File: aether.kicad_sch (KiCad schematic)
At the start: 4 parts, among them U1 LoRa-E5

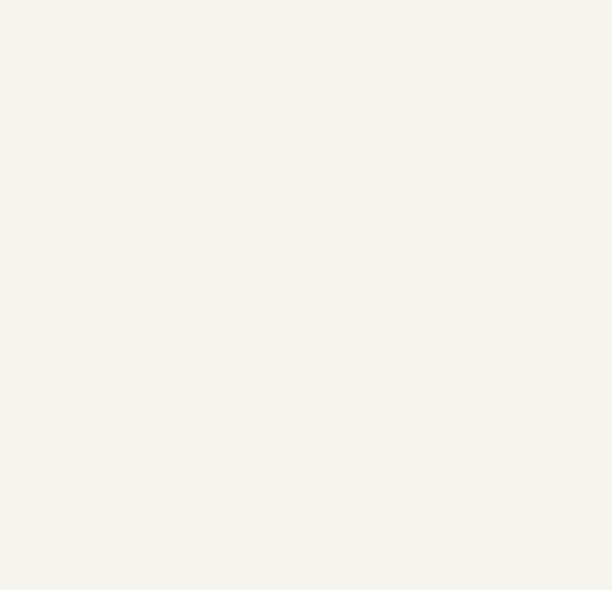
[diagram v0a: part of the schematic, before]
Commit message: Reorganized repo & added power schematic
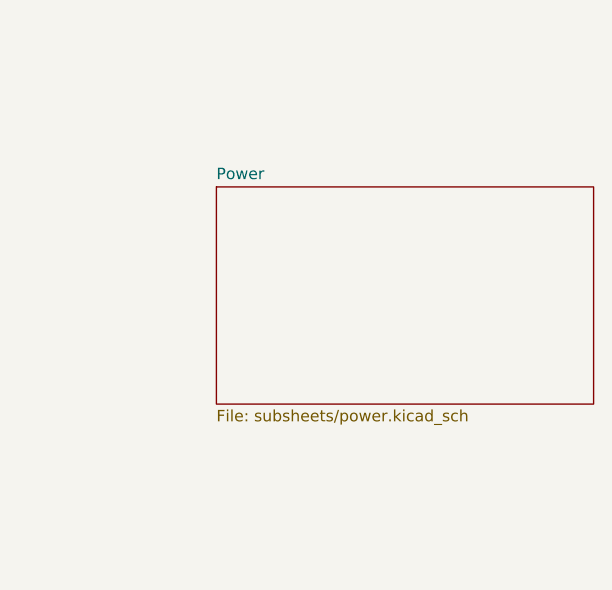
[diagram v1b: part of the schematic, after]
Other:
- added sheet Power (subsheets/power.kicad_sch)

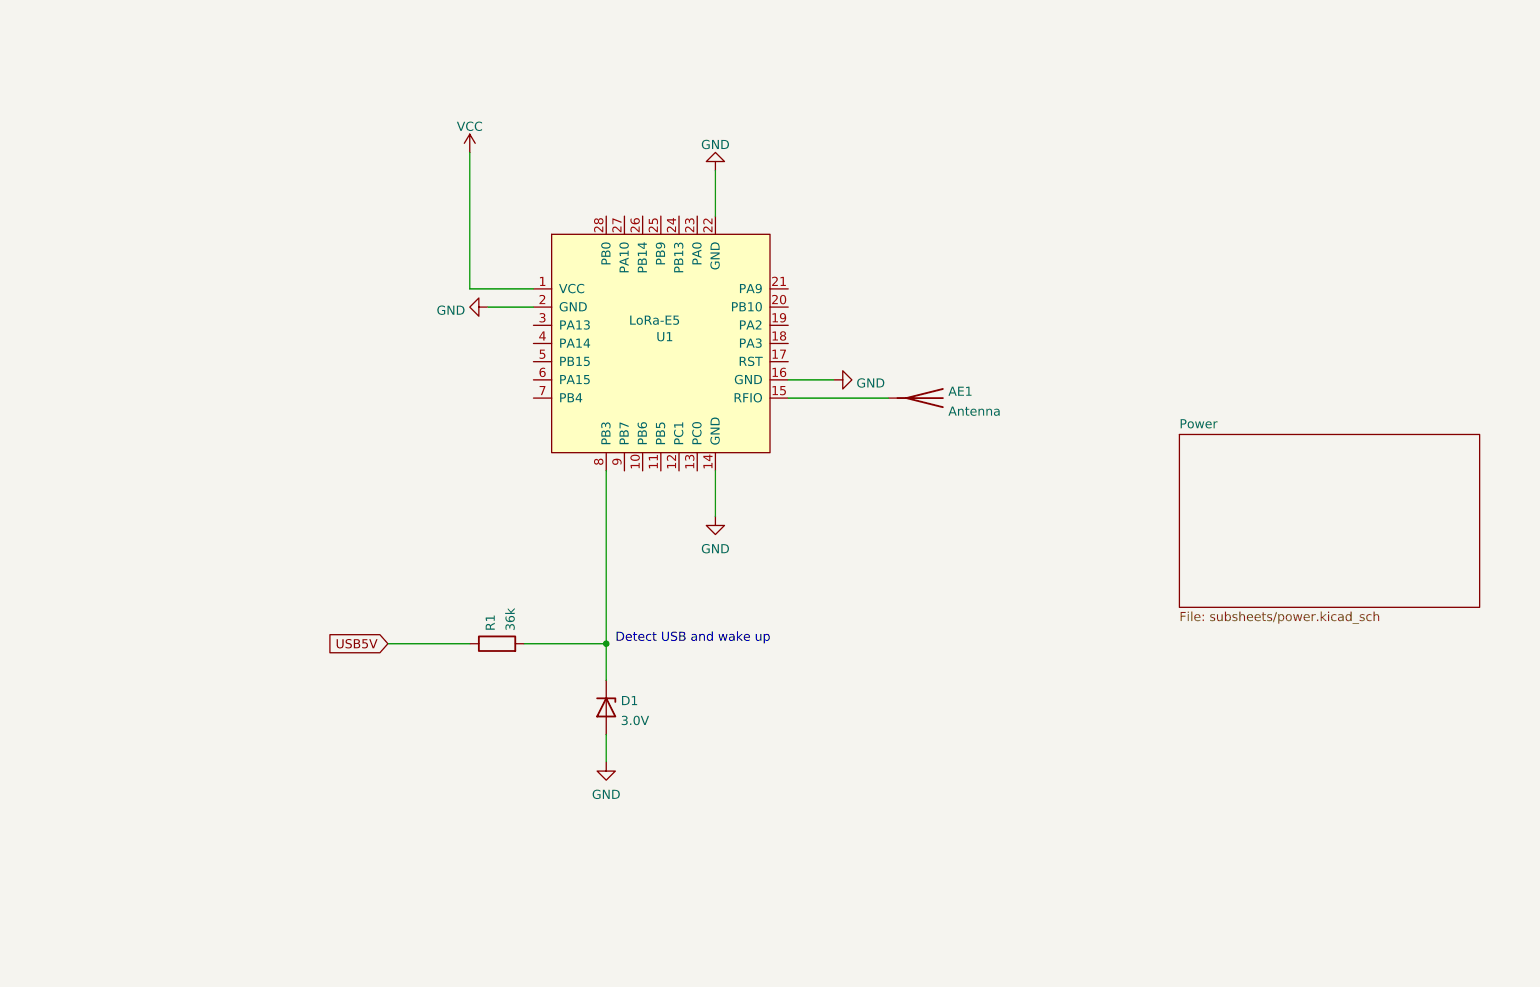
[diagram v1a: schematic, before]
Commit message: Added MCU sch sheet and updated sheet layout
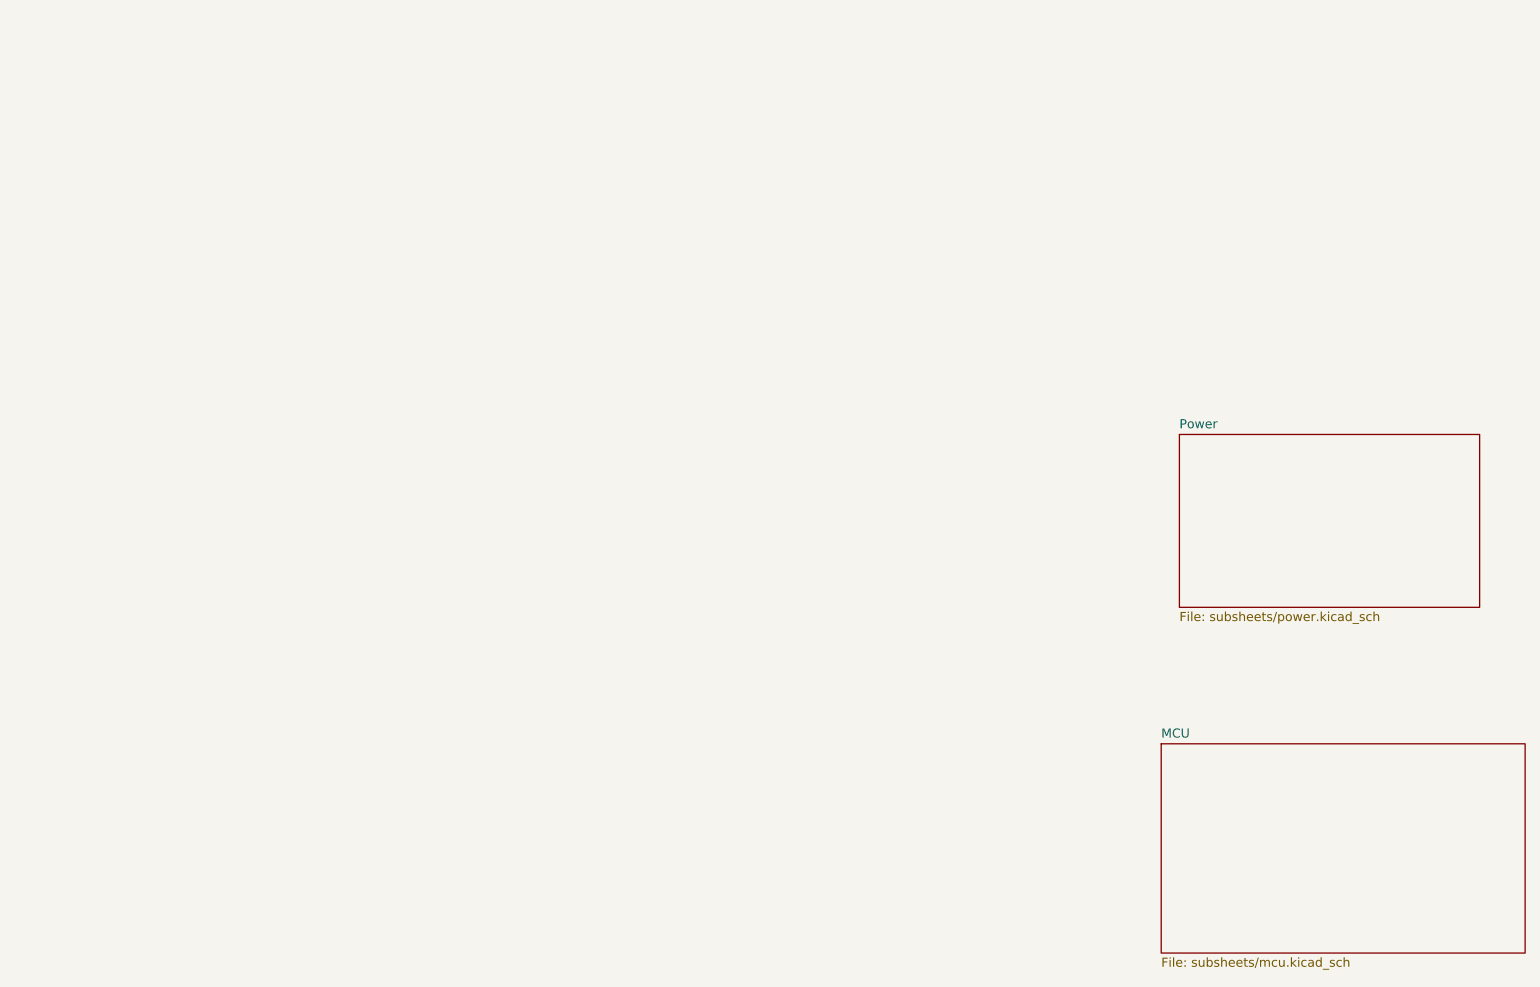
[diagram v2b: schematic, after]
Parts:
- removed AE1: Antenna, symbol Device:Antenna
- removed D1: 3.0V, symbol Device:D_Zener
- removed R1: 36k, symbol Device:R
- removed U1: LoRa-E5, symbol LoRa-E5:LoRa-E5
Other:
- added sheet MCU (subsheets/mcu.kicad_sch)
- note removed: "Detect USB and wake up"
- title: Aether Sensor Network - LoRa Module -> LoRa Module

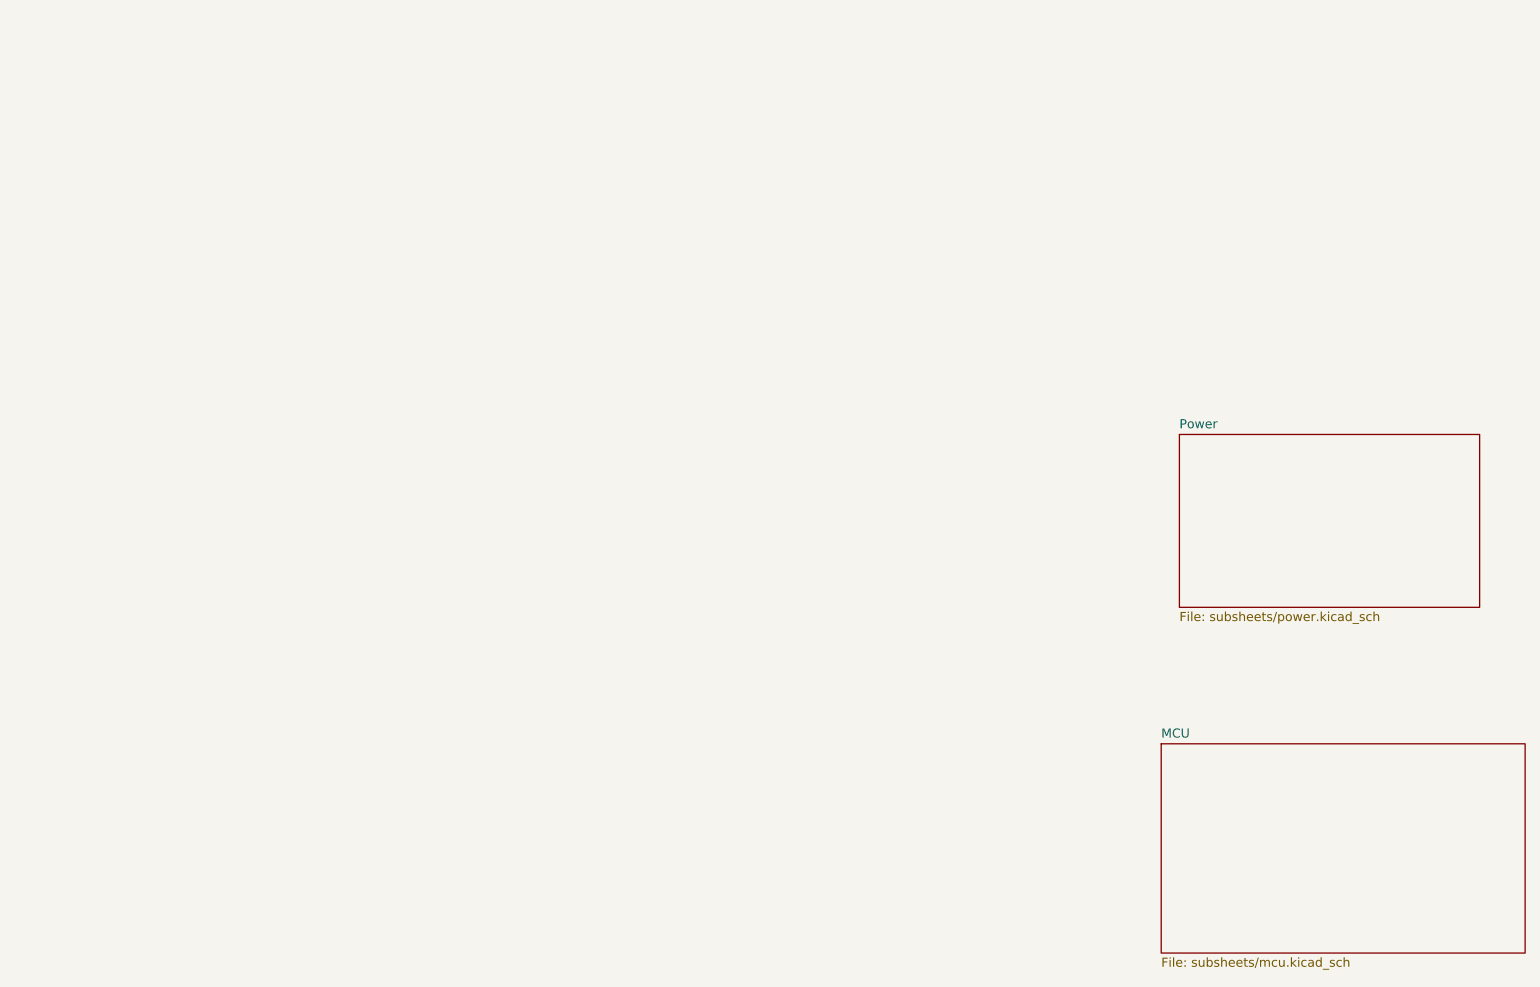
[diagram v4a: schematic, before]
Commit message: USB Comm Interface complete; Sensor and MCU connection complete;
-
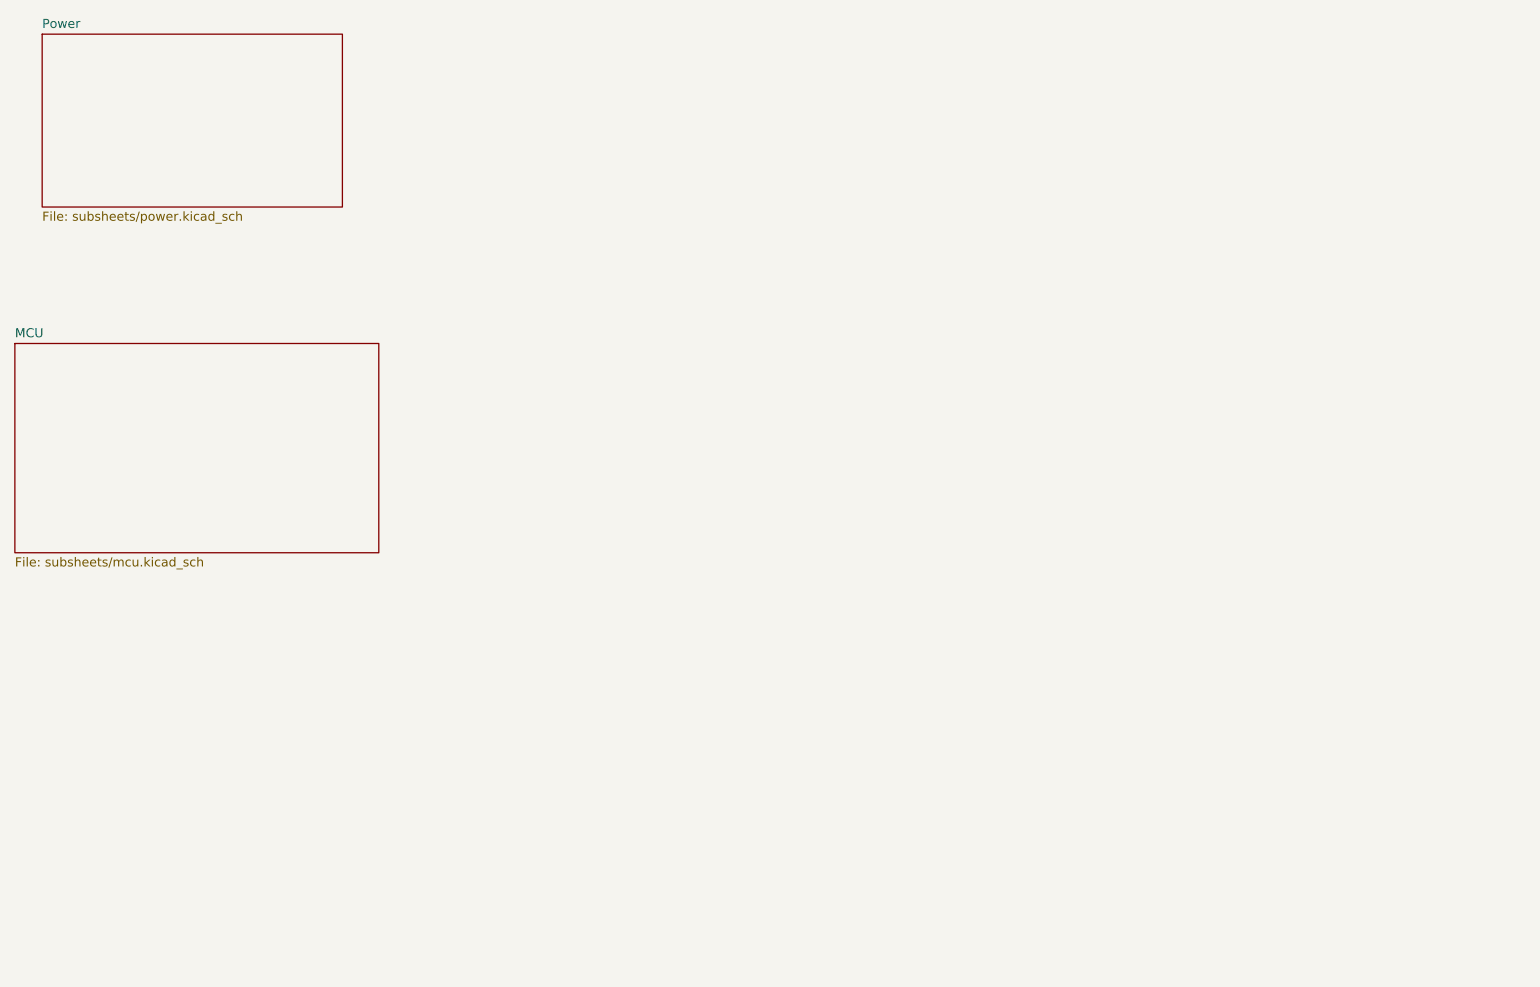
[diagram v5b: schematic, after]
